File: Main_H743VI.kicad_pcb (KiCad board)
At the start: 2 copper layers, 160 x 100 mm, 71 parts, among them J1 ST-LINK, J10 AS7265X, J11 TFT_LCD2, J12 SERVO1, J13 USER_GPIO, J14 TFT_LCD, J15 SERVO2, J16 FAN, J17 ADC_IN, J2 USB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

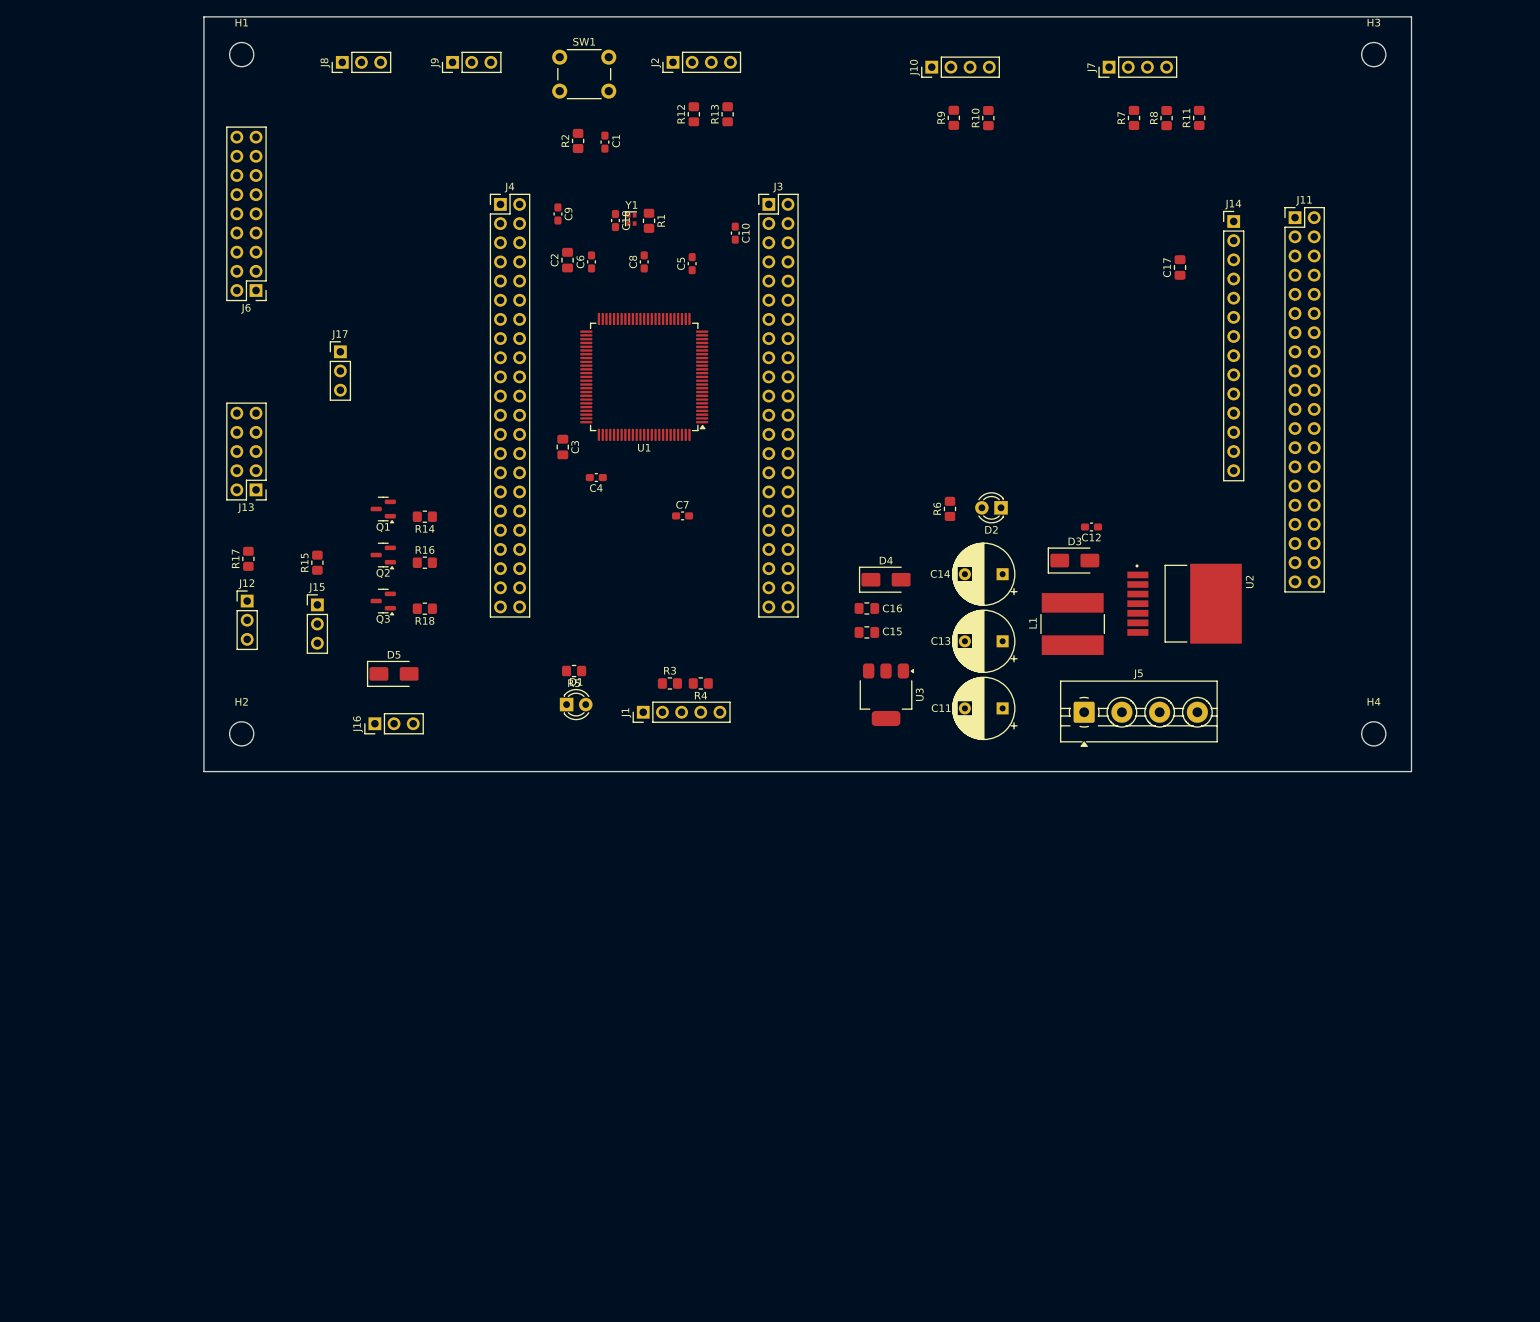
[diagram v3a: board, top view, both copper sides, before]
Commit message: move servo connector closer to power supply
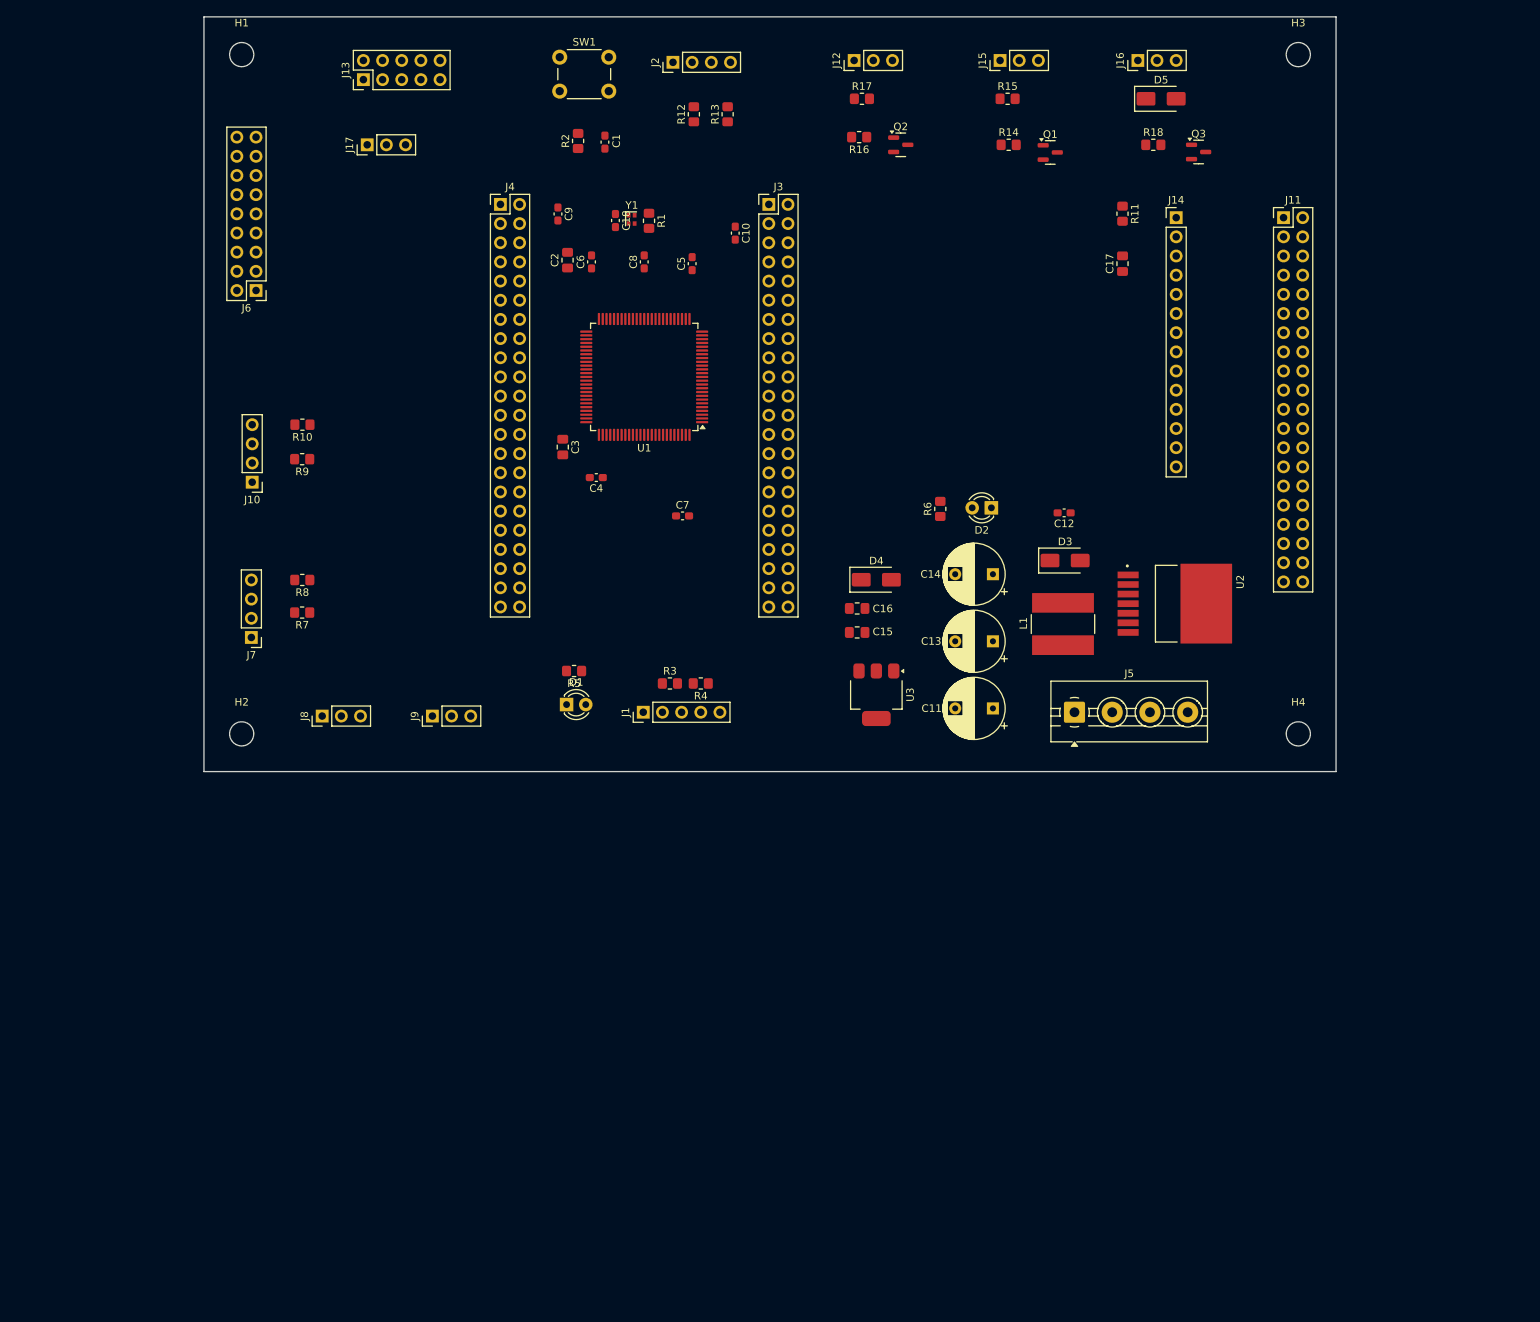
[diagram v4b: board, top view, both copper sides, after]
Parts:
- J8: value Conn_01x03 -> UART1
- J9: value Conn_01x03 -> UART2
- moved J7 136.5 mm to (81.3, 102.2), turned to 180 degrees
- moved J16 134.0 mm to (198.7, 25.8)
- moved R8 129.8 mm to (88.0, 94.6), turned to 180 degrees
- moved R7 128.2 mm to (88.0, 98.9), turned to 180 degrees
- moved D5 127.0 mm to (201.8, 30.9)
- moved Q3 123.3 mm to (206.8, 37.9), turned to 0 degrees
- moved J15 115.7 mm to (180.5, 25.8), turned to 90 degrees
- moved R18 114.4 mm to (200.8, 37.0), turned to 0 degrees
- moved R15 110.2 mm to (181.5, 30.9), turned to 0 degrees
- moved J12 107.7 mm to (161.1, 25.8), turned to 90 degrees
- moved J10 105.5 mm to (81.4, 81.7), turned to 180 degrees
- moved R17 101.6 mm to (162.2, 30.9), turned to 0 degrees
- moved Q1 100.2 mm to (187.1, 38.0), turned to 0 degrees
- moved R10 99.6 mm to (88.0, 74.0), turned to 180 degrees
- moved R9 97.5 mm to (88.0, 78.6), turned to 180 degrees
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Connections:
- J9 pad 3: PA3 -> PD6
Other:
- board size 160 x 100 mm -> 150 x 100 mm

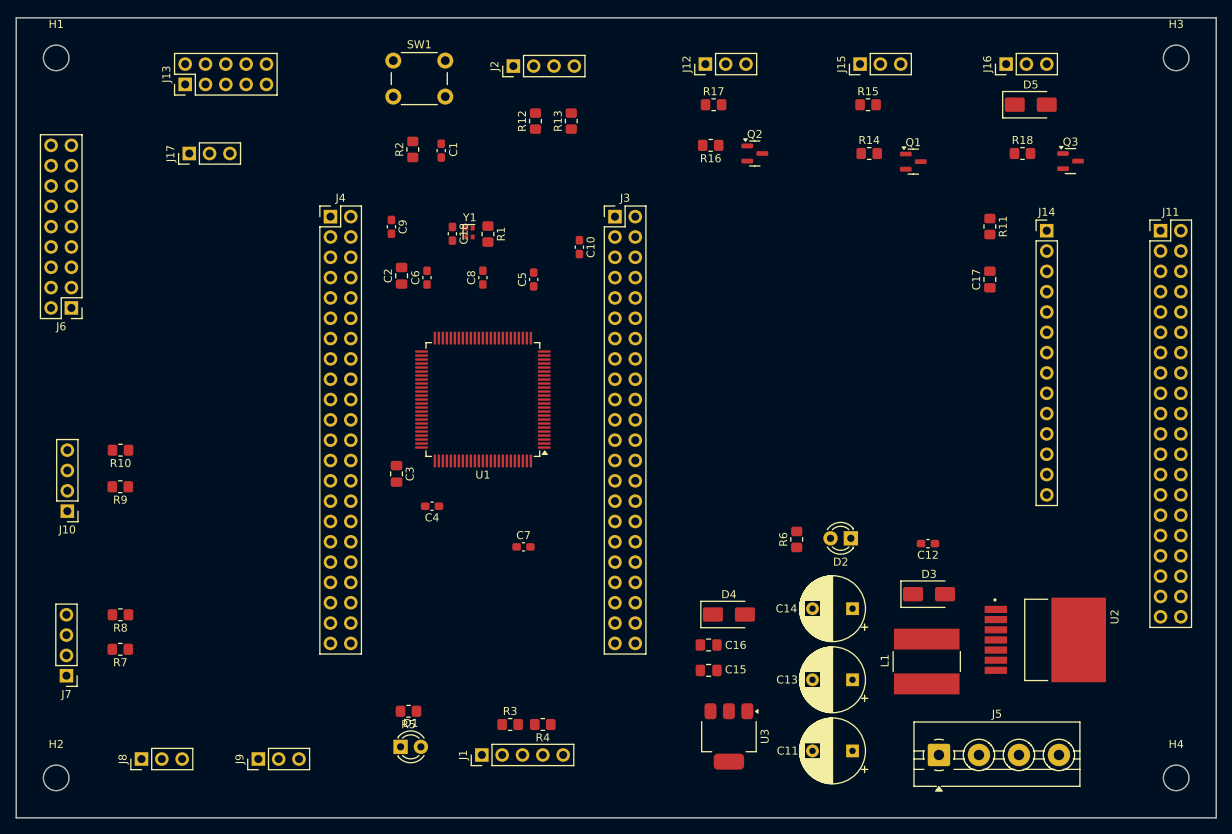
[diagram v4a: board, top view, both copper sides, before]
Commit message: change transistors from MMBT2222A to BCP56
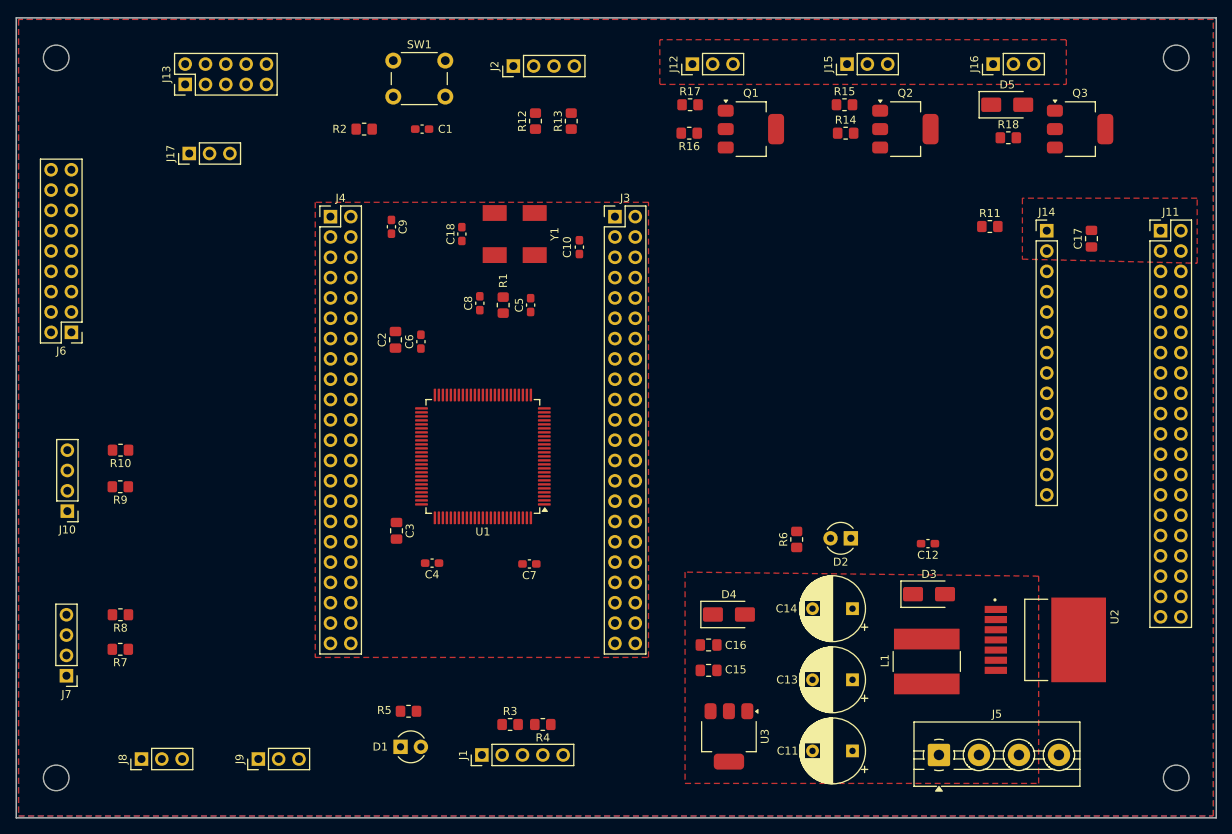
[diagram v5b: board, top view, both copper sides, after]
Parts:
- Q1, Q2, Q3: value MMBT2222A -> BCP56; footprint Package_TO_SOT_SMD:SOT-23 -> Package_TO_SOT_SMD:SOT-223-3_TabPin2
- SW1: value tact switch -> RESET SW
- Y1: footprint Oscillator:Oscillator_SMD_Abracon_ASCO-4Pin_1.6x1.2mm -> Oscillator:Oscillator_SMD_Abracon_ASV-4Pin_7.0x5.1mm_HandSoldering
- moved Q1 20.7 mm to (166.8, 33.9)
- moved Q2 19.1 mm to (186.1, 33.9)
- moved C17 13.7 mm to (209.4, 47.6)
- moved R1 9.08 mm to (135.9, 55.9)
- moved C2 8.04 mm to (122.4, 60.2)
- moved C6 8.04 mm to (125.6, 60.5)
- moved U1 7.11 mm to (133.3, 74.8)
- moved C3 7.11 mm to (122.5, 84.1)
- moved C4 7.11 mm to (127.0, 88.2)
- moved R2 6.59 mm to (118.5, 33.9), turned to 180 degrees
- moved Y1 5.65 mm to (137.3, 47.0), turned to -90 degrees
- moved Q3 4.17 mm to (208.0, 33.9)
- moved R14 3.89 mm to (178.7, 34.4)
- moved C1 3.60 mm to (125.7, 33.9), turned to 180 degrees
- moved C5 3.22 mm to (139.3, 55.9)
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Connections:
- Q1 pad 2: GND -> Net-(J12-Pin_3)
- Q1 pad 3: Net-(J12-Pin_3) -> GND
- Q2 pad 2: GND -> Net-(J15-Pin_3)
- Q2 pad 3: Net-(J15-Pin_3) -> GND
- Q3 pad 2: GND -> Net-(D5-A)
- Q3 pad 3: Net-(D5-A) -> GND
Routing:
- added copper zone on F.Cu, net +3.3V
- added copper zone on B.Cu, net GND
- added copper zone on F.Cu, net GND
- added copper zone on F.Cu, net VCC
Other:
- copper layers 2 -> 4

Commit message: move diode closer to +5V
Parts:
- moved D4 49.7 mm to (160.1, 45.1), turned to 180 degrees
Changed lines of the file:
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@@
 	(footprint "Diode_SMD:D_SMA"
 		(layer "F.Cu")
-		(at 164.091 94.5775)
+		(at 160.1 45.08 180)
 		(descr "Diode SMA (DO-214AC)")
 		(tags "Diode SMA (DO-214AC)")
@@
 		)
 		(property "Datasheet" "https://www.vishay.com/docs/88751/ss32.pdf"
-			(at 0 0 0)
+			(at 0 0 180)
 			(unlocked yes)
 			(layer "F.Fab")
@@
 		)
 		(property "Description" "60V 3A Schottky Diode, SMA"
-			(at 0 0 0)
+			(at 0 0 180)
 			(unlocked yes)
 			(layer "F.Fab")
@@
 		(attr smd)
 		(fp_line
+			(start -3.51 1.65)
+			(end 2 1.65)
+			(stroke
+				(width 0.12)
+				(type solid)
+			)
+			(layer "F.SilkS")
+		)
+		(fp_line
+			(start -3.51 -1.65)
+			(end 2 -1.65)
+			(stroke
+				(width 0.12)
+				(type solid)
+			)
+			(layer "F.SilkS")
+		)
+		(fp_line
 			(start -3.51 -1.65)
 			(end -3.51 1.65)
@@
 		)
 		(fp_line
-			(start -3.51 -1.65)
-			(end 2 -1.65)
-			(stroke
-				(width 0.12)
-				(type solid)
-			)
-			(layer "F.SilkS")
-		)
-		(fp_line
-			(start -3.51 1.65)
-			(end 2 1.65)
-			(stroke
-				(width 0.12)
-				(type solid)
-			)
-			(layer "F.SilkS")
+			(start 3.5 1.75)
+			(end -3.5 1.75)
+			(stroke
+				(width 0.05)
+				(type solid)
+			)
+			(layer "F.CrtYd")
+		)
+		(fp_line
+			(start 3.5 -1.75)
+			(end 3.5 1.75)
+			(stroke
+				(width 0.05)
+				(type solid)
+			)
+			(layer "F.CrtYd")
+		)
+		(fp_line
+			(start -3.5 1.75)
+			(end -3.5 -1.75)
+			(stroke
+				(width 0.05)
+				(type solid)
+			)
+			(layer "F.CrtYd")
 		)
 		(fp_line
@@
 		)
 		(fp_line
-			(start -3.5 1.75)
-			(end -3.5 -1.75)
-			(stroke
-				(width 0.05)
-				(type solid)
-			)
-			(layer "F.CrtYd")
-		)
-		(fp_line
-			(start 3.5 -1.75)
-			(end 3.5 1.75)
-			(stroke
-				(width 0.05)
-				(type solid)
-			)
-			(layer "F.CrtYd")
-		)
-		(fp_line
-			(start 3.5 1.75)
-			(end -3.5 1.75)
-			(stroke
-				(width 0.05)
-				(type solid)
-			)
-			(layer "F.CrtYd")
+			(start 2.3 1.5)
+			(end -2.3 1.5)
+			(stroke
+				(width 0.1)
+				(type solid)
+			)
+			(layer "F.Fab")
+		)
+		(fp_line
+			(start 2.3 -1.5)
+			(end 2.3 1.5)
+			(stroke
+				(width 0.1)
+				(type solid)
+			)
+			(layer "F.Fab")
+		)
+		(fp_line
+			(start 2.3 -1.5)
+			(end -2.3 -1.5)
+			(stroke
+				(width 0.1)
+				(type solid)
+			)
+			(layer "F.Fab")
+		)
+		(fp_line
+			(start 0.50118 0.75032)
+			(end 0.50118 -0.79908)
+			(stroke
+				(width 0.1)
+				(type solid)
+			)
+			(layer "F.Fab")
+		)
+		(fp_line
+			(start 0.50118 0.00102)
+			(end 1.4994 0.00102)
+			(stroke
+				(width 0.1)
+				(type solid)
+			)
+			(layer "F.Fab")
+		)
+		(fp_line
+			(start -0.64944 0.00102)
+			(end 0.50118 0.75032)
+			(stroke
+				(width 0.1)
+				(type solid)
+			)
+			(layer "F.Fab")
+		)
+		(fp_line
+			(start -0.64944 0.00102)
+			(end 0.50118 -0.79908)
+			(stroke
+				(width 0.1)
+				(type solid)
+			)
+			(layer "F.Fab")
+		)
+		(fp_line
+			(start -0.64944 0.00102)
+			(end -1.55114 0.00102)
+			(stroke
+				(width 0.1)
+				(type solid)
+			)
+			(layer "F.Fab")
+		)
+		(fp_line
+			(start -0.64944 -0.79908)
+			(end -0.64944 0.80112)
+			(stroke
+				(width 0.1)
+				(type solid)
+			)
+			(layer "F.Fab")
 		)
 		(fp_line
@@
 			(layer "F.Fab")
 		)
-		(fp_line
-			(start -0.64944 -0.79908)
-			(end -0.64944 0.80112)
-			(stroke
-				(width 0.1)
-				(type solid)
-			)
-			(layer "F.Fab")
-		)
-		(fp_line
-			(start -0.64944 0.00102)
-			(end -1.55114 0.00102)
-			(stroke
-				(width 0.1)
-				(type solid)
-			)
-			(layer "F.Fab")
-		)
-		(fp_line
-			(start -0.64944 0.00102)
-			(end 0.50118 -0.79908)
-			(stroke
-				(width 0.1)
-				(type solid)
-			)
-			(layer "F.Fab")
-		)
-		(fp_line
-			(start -0.64944 0.00102)
-			(end 0.50118 0.75032)
-			(stroke
-				(width 0.1)
-				(type solid)
-			)
-			(layer "F.Fab")
-		)
-		(fp_line
-			(start 0.50118 0.00102)
-			(end 1.4994 0.00102)
-			(stroke
-				(width 0.1)
-				(type solid)
-			)
-			(layer "F.Fab")
-		)
-		(fp_line
-			(start 0.50118 0.75032)
-			(end 0.50118 -0.79908)
-			(stroke
-				(width 0.1)
-				(type solid)
-			)
-			(layer "F.Fab")
-		)
-		(fp_line
-			(start 2.3 -1.5)
-			(end -2.3 -1.5)
-			(stroke
-				(width 0.1)
-				(type solid)
-			)
-			(layer "F.Fab")
-		)
-		(fp_line
-			(start 2.3 -1.5)
-			(end 2.3 1.5)
-			(stroke
-				(width 0.1)
-				(type solid)
-			)
-			(layer "F.Fab")
-		)
-		(fp_line
-			(start 2.3 1.5)
-			(end -2.3 1.5)
-			(stroke
-				(width 0.1)
-				(type solid)
-			)
-			(layer "F.Fab")
-		)
 		(fp_text user "${REFERENCE}"
 			(at 0 -2.5 0)
@@
 		)
 		(pad "1" smd roundrect
-			(at -2 0)
+			(at -2 0 180)
 			(size 2.5 1.8)
 			(layers "F.Cu" "F.Mask" "F.Paste")
@@
 		)
 		(pad "2" smd roundrect
-			(at 2 0)
+			(at 2 0 180)
 			(size 2.5 1.8)
 			(layers "F.Cu" "F.Mask" "F.Paste")
